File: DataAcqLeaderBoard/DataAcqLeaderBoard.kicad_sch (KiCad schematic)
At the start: 79 parts, among them J10 PWR_IN, J2 RF_UART, J3 LTE_UART, J4 LTE_Trace, J5 GPS_I2C, J6 PWR_OUT, J7 ICAN_IN, J8 CCAN_IN, J9 CCAN_OUT, Q1 NMOS, Q2 NMOS, SW1 RF_RESET, SW2 RF_COM, SW3 LTE_RESET, SW4 GPS_RESET, U1 PA1616S_GPS, X1 DigiXBeeRX900Micro, X2 DigiXBee3LTECat4

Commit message: Completed BOM & Filled out PR template
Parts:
- removed D1: RF_COM, LED_SMD:LED_0805_2012Metric, symbol Device:LED
- removed R9: 1k, Resistor_SMD:R_0805_2012Metric, symbol Device:R
- added LOGO1: Otter, DataAcqLeaderBoard-Footprints:otter, symbol utsvt-misc:Logo_Placeholder
- added LOGO2: UTSVT, UTSVT_Special:UTSVT_Logo_Symbol, symbol utsvt-misc:Logo_Placeholder
- added LOGO3: Sun, DataAcqLeaderBoard-Footprints:sun, symbol utsvt-misc:Logo_Placeholder
- BAT1: Link (none) -> https://www.mouser.com/ProductDetail/Keystone-Electronics/2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; Mouser Part Number https://www.mouser.com/ProductDetail/Keystone-Electronics/2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 -> 534-2994TR; P/N (none) -> 2994TR
- C1, C9: Link (none) -> https://www.mouser.com/ProductDetail/KYOCERA-AVX/TCP0J106M8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; Mouser Part Number (none) -> 755-TCP0J106M8R; P/N (none) -> TCP0J106M8R
- C10, C13: Link (none) -> https://www.mouser.com/ProductDetail/KEMET/C0805C103F8HACAU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; Mouser Part Number (none) -> 80-C0805C103F8HAUTO; P/N (none) -> C0805C103F8HACAUTO
- C11: Link (none) -> https://www.mouser.com/ProductDetail/KEMET/C0805C560FBGACTU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; Mouser Part Number (none) -> 80-C0805C560FBG; P/N (none) -> C0805C560FBGACTU
- C12: Link (none) -> https://www.mouser.com/ProductDetail/KEMET/C0805C100F1GACTU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; Mouser Part Number (none) -> 80-C0805C100F1GACTU; P/N (none) -> C0805C100F1GACTU
- C14, C15, C17, C18, C2, C4, C5: Link (none) -> https://www.mouser.com/ProductDetail/KEMET/C0805C105J4RAC72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; Mouser Part Number (none) -> 80-C0805C105J4RACLR; P/N (none) -> C0805C105J4RAC7210
- C16: value 0.1u -> 100n; Link (none) -> https://www.mouser.com/ProductDetail/KEMET/C0805C104M5RACTU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; Mouser Part Number (none) -> 80-C0805C104M5R; P/N (none) -> C0805C104M5RACTU
- C3: Link (none) -> https://www.mouser.com/ProductDetail/KEMET/C0805C470F5GACTU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; Mouser Part Number (none) -> 80-C0805C470F5G; P/N (none) -> C0805C470F5GACTU
- C6, C7, C8: Link (none) -> https://www.mouser.com/ProductDetail/KYOCERA-AVX/TCTPL0G107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; Mouser Part Number (none) -> 755-TCTPL0G107M8R-V1; P/N (none) -> TCTPL0G107M8R-V1
- D1: renamed from D2; value RF_MOD -> RF_COM_LED; Link (none) -> https://www.mouser.com/ProductDetail/Kingbright/APTD2012LCG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; P/N (none) -> APTD2012LCGCK
- D2: renamed from D3; Link (none) -> https://www.mouser.com/ProductDetail/Kingbright/APTD2012LCG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; P/N (none) -> APTD2012LCGCK
- D3: renamed from D4; Link (none) -> https://www.mouser.com/ProductDetail/Kingbright/APTD2012LCG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; P/N (none) -> APTD2012LCGCK
- D4: renamed from D5; Link (none) -> https://www.mouser.com/ProductDetail/Kingbright/APTD2012LCG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; P/N (none) -> APTD2012LCGCK
- D5: renamed from D6; Link (none) -> https://www.mouser.com/ProductDetail/Kingbright/APTD2012LCG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; P/N (none) -> APTD2012LCGCK
- D6: renamed from D7; Link (none) -> https://www.mouser.com/ProductDetail/Kingbright/APTD2012LCG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; P/N (none) -> APTD2012LCGCK
- D7: renamed from D8; Link (none) -> https://www.mouser.com/ProductDetail/Kingbright/APTD2012LCG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; P/N (none) -> APTD2012LCGCK
- D8: renamed from D9; Link (none) -> https://www.mouser.com/ProductDetail/Kingbright/APTD2012LCG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; P/N (none) -> APTD2012LCGCK
- FB1: Link (none) -> https://www.digikey.com/en/products/detail/pulse-electronic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; Mouser Part Number https://www.digikey.com/en/products/detail/pulse-electronic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 -> (none); P/N (none) -> GMLB-100505-0600A-N8
- J1: Link (none) -> https://www.mouser.com/ProductDetail/Molex/53307-2471?qs=3D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; Mouser Part Number (none) -> 538-53307-2471; P/N (none) -> 53307-2471
- J10, J6, J7, J8, J9: Link (none) -> https://www.mouser.com/ProductDetail/538-43650-0215; Mouser Part Number (none) -> 538-43650-0215; P/N (none) -> 43650-0215
- J2, J3, J5: Link (none) -> https://www.mouser.com/ProductDetail/Molex/22-28-4035?qs=GA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; Mouser Part Number (none) -> 538-22-28-4035; P/N (none) -> 22-28-4035
- J4: Link (none) -> https://www.mouser.com/ProductDetail/Molex/22-28-4045?qs=Mu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; Mouser Part Number (none) -> 538-22-28-4045; P/N (none) -> 22-28-4045
- Q1, Q2: Link (none) -> https://www.mouser.com/ProductDetail/Infineon-Technologies/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; Mouser Part Number (none) -> 942-IRLML0030TRPBF; P/N (none) -> IRLML0030TRPBF
- R1, R13, R16, R17, R18, R19, R2, R20, R24, R25, R3, R4, R5, R7: Link (none) -> https://www.mouser.com/ProductDetail/Vishay-Dale/CRCW080510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; P/N (none) -> CRCW080510K0FKEA
- R10, R11, R12, R14, R15, R21, R22, R23, R26, R27, R6, R8: Link (none) -> https://www.mouser.com/ProductDetail/Vishay-Dale/CRCW08051K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; Mouser Part Number (none) -> 71-CRCW08051K00FKEAC; P/N (none) -> CRCW08051K00FKEAC
- R28: Link (none) -> https://www.mouser.com/ProductDetail/Vishay-Dale/CRCW080510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; Mouser Part Number (none) -> 71-CRCW080510K0FKEAC; P/N (none) -> CRCW080510K0FKEA
- SW1: Link (none) -> https://www.mouser.com/ProductDetail/Omron-Electronics/B3SL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; P/N (none) -> B3SL-1002P
- SW2, SW3, SW4: Link (none) -> https://www.mouser.com/ProductDetail/Omron-Electronics/B3SL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; Mouser Part Number (none) -> 653-B3SL-1002P; P/N (none) -> B3SL-1002P
- U1: Link (none) -> https://www.adafruit.com/product/790?gad_source=1&gclid=Cj0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; Mouser Part Number https://www.adafruit.com/product/790?gad_source=1&gclid=Cj0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 -> (none); P/N (none) -> PA1616S
- X1: Link (none) -> https://www.digi.com/products/embedded-systems/digi-xbee/rf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; P/N (none) -> XB-9XR-DMRM-001
- X2: Link (none) -> https://www.digi.com/products/embedded-systems/digi-xbee/ce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; P/N (none) -> XB3-C-G4-UT-001
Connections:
- net LTE_D8 is gone; now on net LTE_D7: D7.2 (A), R23.2
- net RF_D4 is gone; now on net RF_D3: D3.2 (A), R12.2
- net LTE_D5: now also D5.2 (A), R15.2; no longer D4.2 (A), R14.2
- net LTE_D6: now also D6.2 (A), R22.2; no longer D5.2 (A), R15.2
- net LTE_D7: no longer D6.2 (A), R22.2
- net RF_D2: now also D2.2 (A), R11.2; no longer D1.2 (A), R10.2
- net RF_D3: no longer D2.2 (A), R11.2
- net GPS_D9 renamed GPS_D8
- net RF_STATUS_COMMISION: no longer names the net of X1.15 (ASSOCIATE/SPI_MOSI/DIO16)
- net RF_STATUS_MODULE renamed RF_COMISSION_LED
- new net LTE_D4: D4.2 (A), R14.2
- new net RF_D21: D1.2 (A), R10.2
- no-connect marks 17 -> 18
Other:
- note added: "MISC"
- note removed: "Mouting"
- moved on the sheet: H1, H2, H3

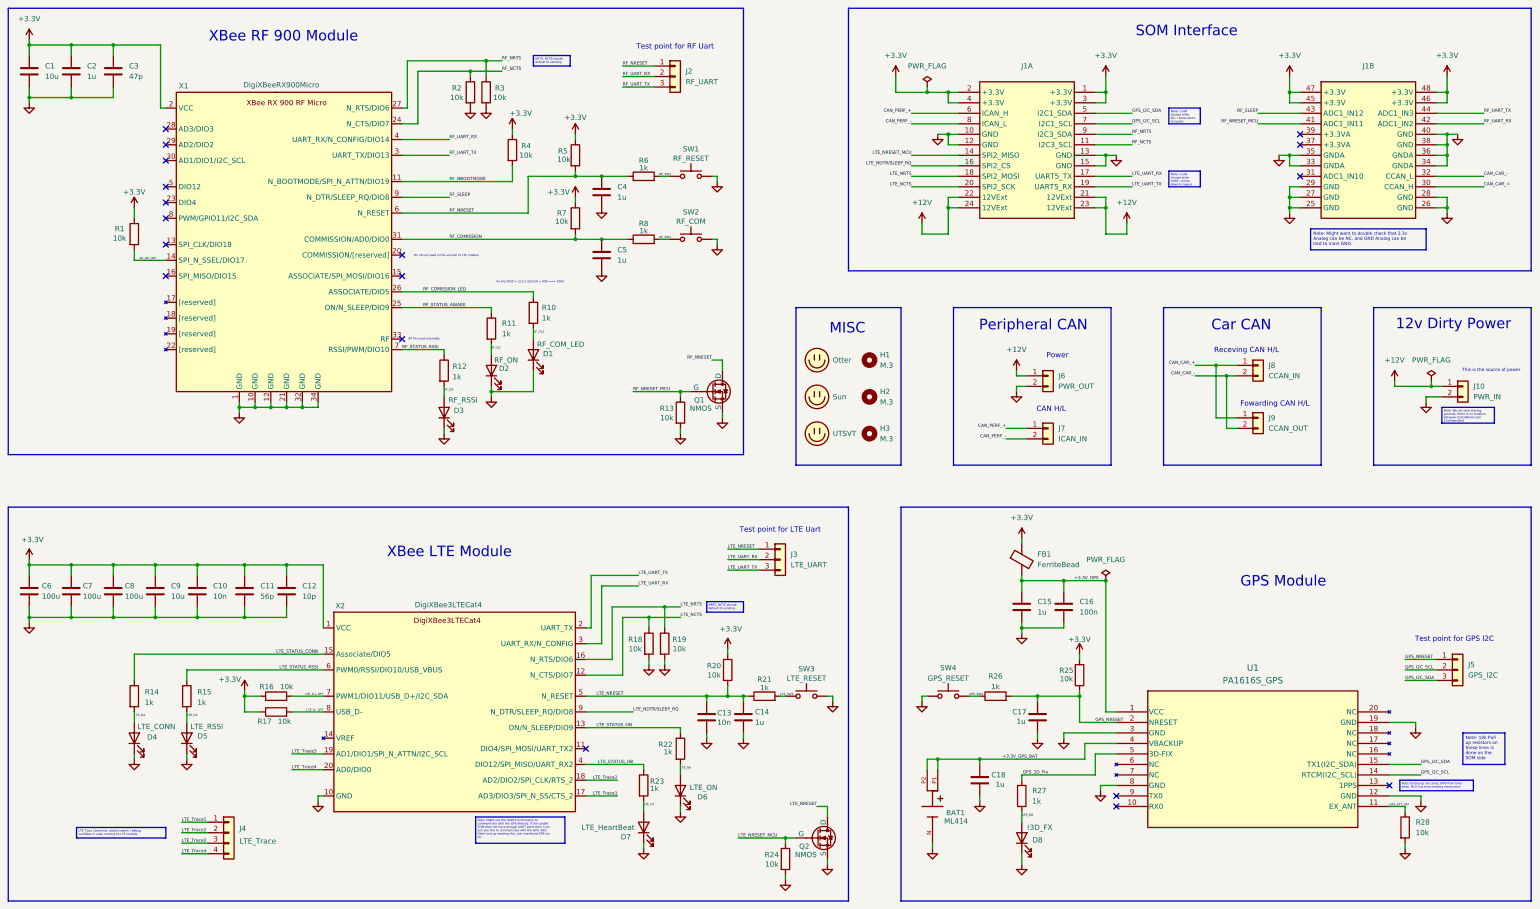
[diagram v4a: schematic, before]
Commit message: Addressed PR comments (vias, test points, labels)
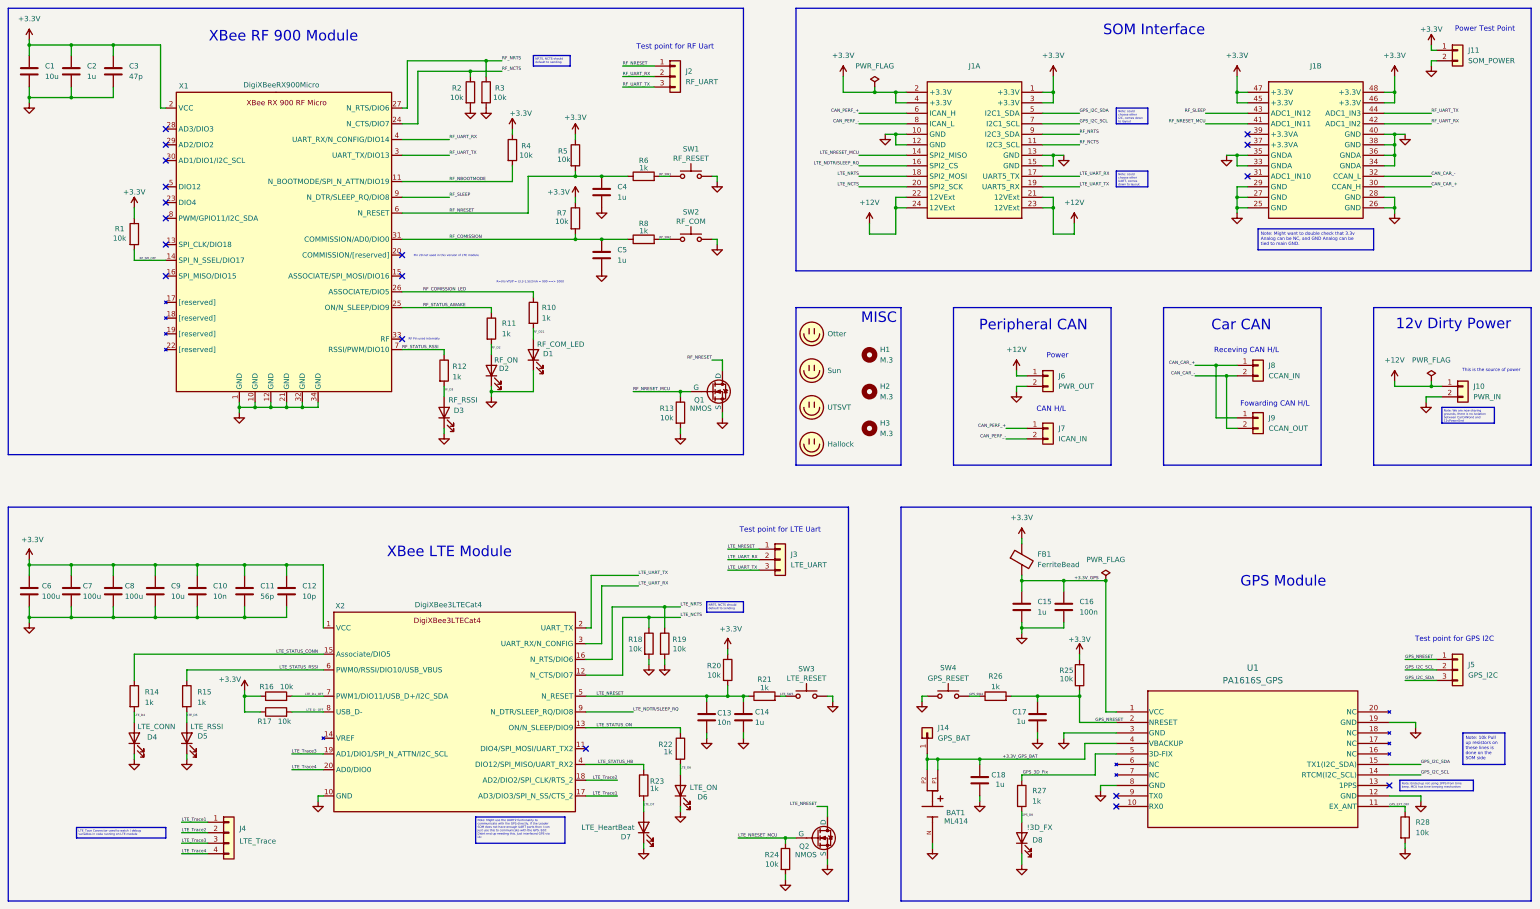
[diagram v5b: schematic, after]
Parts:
- added J11: SOM_POWER, Connector_PinHeader_2.54mm:PinHeader_1x02_P2.54mm_Vertical, symbol Connector_Generic:Conn_01x02
- added J14: GPS_BAT, UTSVT_Special:TestPoint_HEX_3mmID, symbol Connector_Generic:Conn_01x01
- added LOGO4: Hallock, UTSVT_Special:Hallock_Image_Tiny, symbol utsvt-misc:Logo_Placeholder
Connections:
- net +3.3V: now also J11.1 (Pin_1)
- net +3.3V_GPS_BAT: now also J14.1 (Pin_1)
- net GND: now also J11.2 (Pin_2)
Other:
- note added: "Power Test Point"
- moved on the sheet: H1, H2, H3, J1A, J1B

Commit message: Shifted GPS module down for more USB clearance
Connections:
- net GPS_I2C_SCL: now also J5.3 (Pin_3); no longer J5.2 (Pin_2)
- net GPS_I2C_SDA: now also J5.2 (Pin_2); no longer J5.3 (Pin_3)
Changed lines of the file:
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@@
-		)
-	)
-	(label "GPS_I2C_SCL"
-		(at 363.22 185.42 0)
-		(fields_autoplaced yes)
-		(effects
-			(font
-				(size 0.762 0.762)
-			)
-			(justify left bottom)
 		)
 	)
@@
 		)
 	)
+	(label "GPS_I2C_SDA"
+		(at 363.22 185.42 0)
+		(fields_autoplaced yes)
+		(effects
+			(font
+				(size 0.762 0.762)
+			)
+			(justify left bottom)
+		)
+	)
+	(label "GPS_I2C_SCL"
+		(at 363.22 187.96 0)
+		(fields_autoplaced yes)
+		(effects
+			(font
+				(size 0.762 0.762)
+			)
+			(justify left bottom)
+		)
+	)
 	(label "RF_NRTS"
 		(at 284.48 55.88 0)
@@
 		(fields_autoplaced yes)
 		(effects
-			(font
-				(size 0.762 0.762)
-			)
-			(justify left bottom)
-		)
-	)
-	(label "GPS_I2C_SDA"
-		(at 363.22 187.96 0)
-		(fields_autoplaced yes)
-		(effects
